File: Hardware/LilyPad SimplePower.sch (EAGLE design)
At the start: 22 parts, among them U1 MCP73831

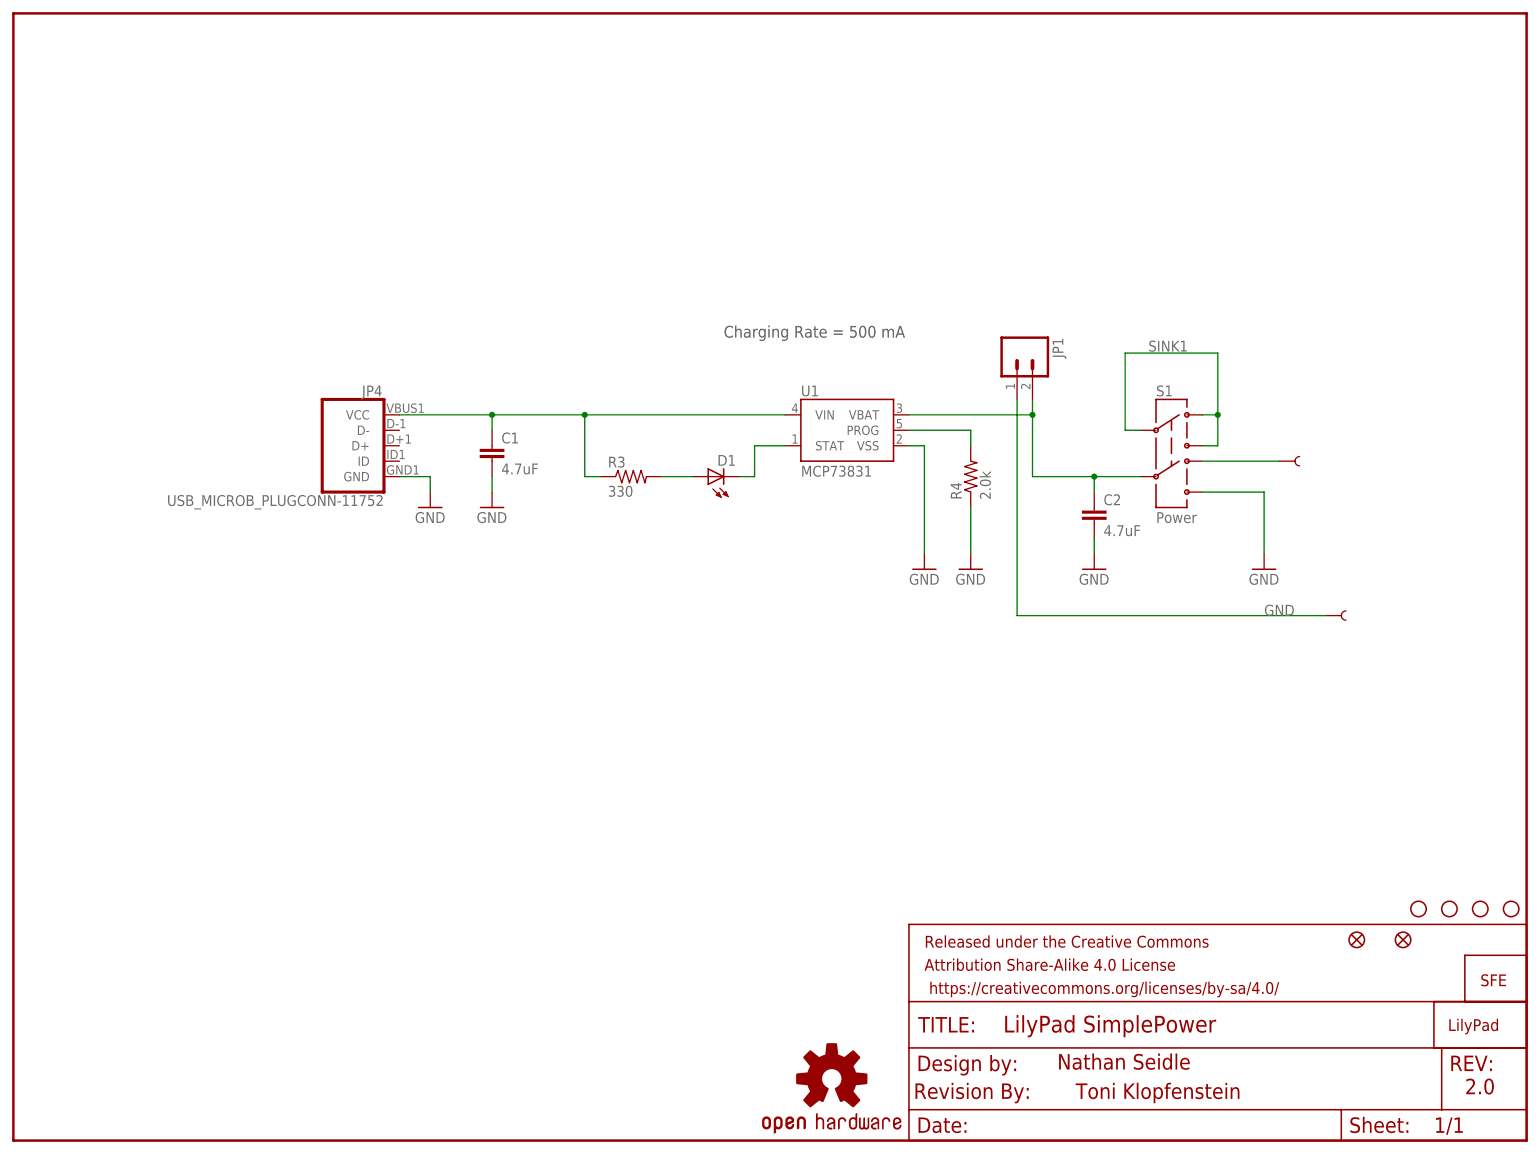
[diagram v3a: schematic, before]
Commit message: Fixing short, updating parts to match QC checklist
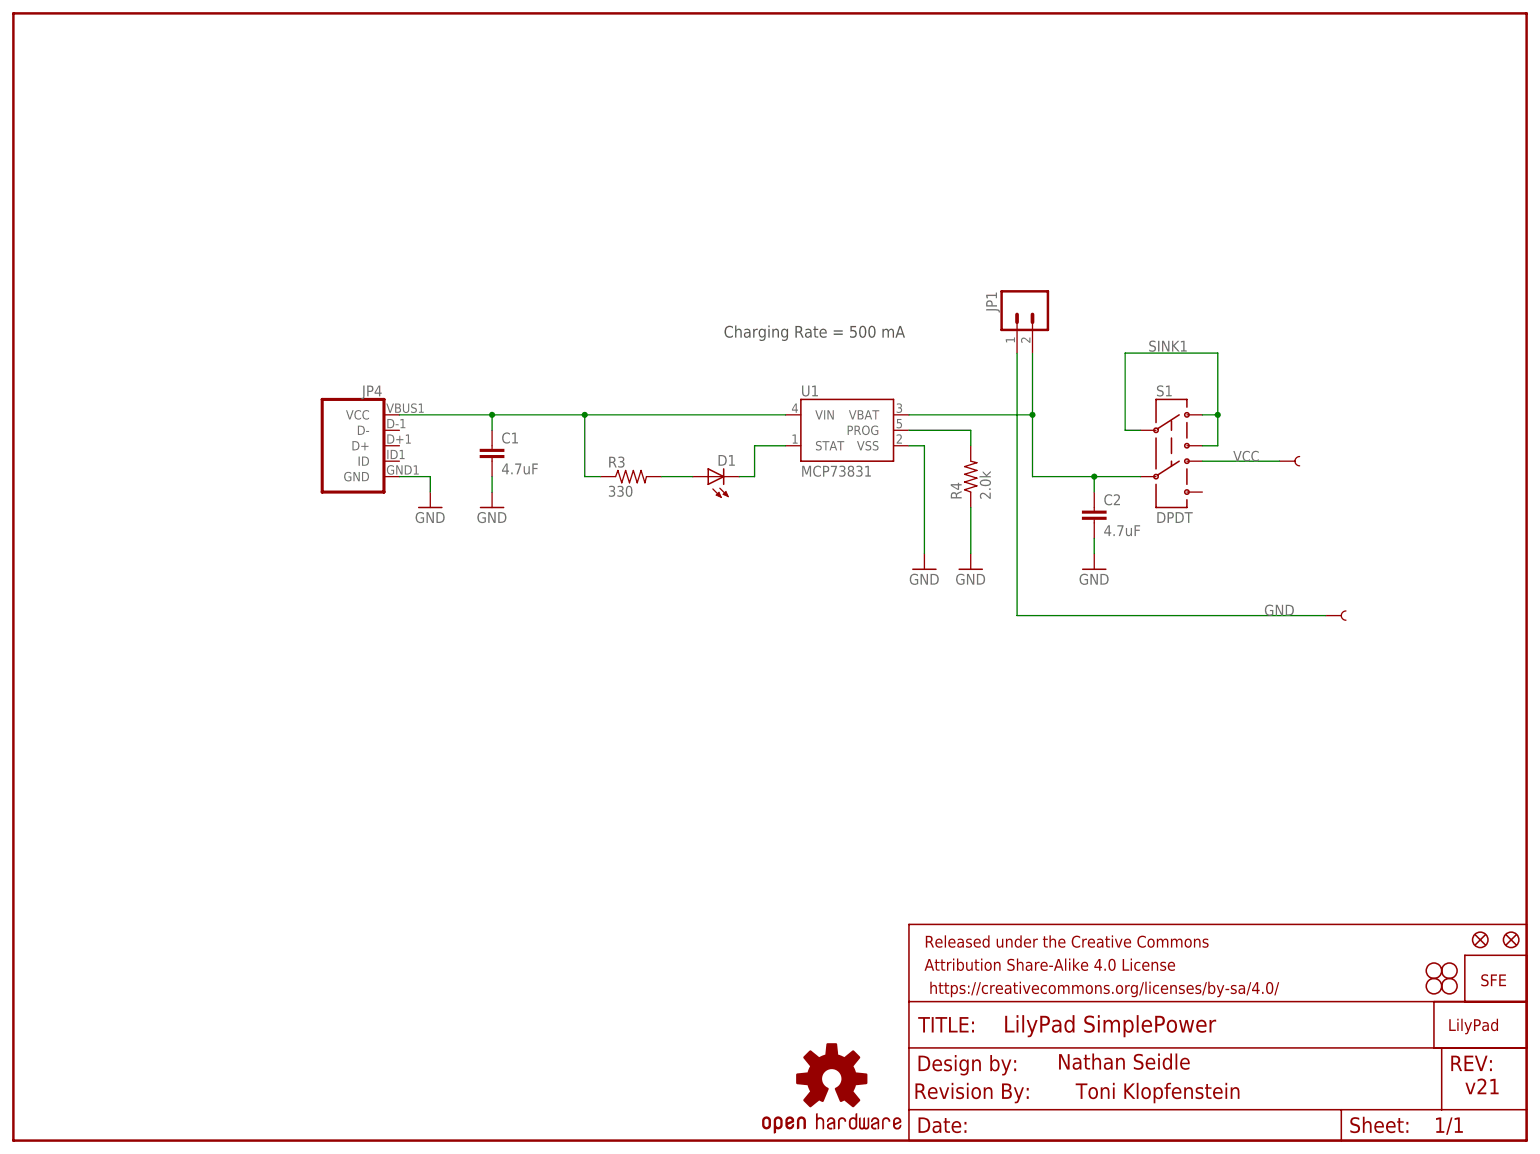
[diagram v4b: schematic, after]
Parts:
- JP1: value (none) -> M02-JST-2MM-SMT; device SparkFun:M02-JST-2MM-SMT -> SparkFun-Connectors:M02-JST-2MM-SMT
- S1: value Power -> DPDT; device SparkFun:SWITCH-DPDTSMD -> SparkFun-Electromechanical:SWITCH-DPDTAYZ0202
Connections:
- net N$6 renamed VCC
- net GND: now also JP1.2; no longer JP1.1, S1.6
- net N$1: now also JP1.1; no longer JP1.2
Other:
- note added: "v21"
- note removed: "2.0"
- moved on the sheet: JP1
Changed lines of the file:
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@@
 <?xml version="1.0" encoding="utf-8"?>
 <!DOCTYPE eagle SYSTEM "eagle.dtd">
-<eagle version="6.6.0">
+<eagle version="7.2.0">
 <drawing>
 <settings>
@@
 <layer number="56" name="wert" color="7" fill="1" visible="no" active="no"/>
 <layer number="57" name="tCAD" color="7" fill="1" visible="no" active="no"/>
+<layer number="90" name="Modules" color="5" fill="1" visible="yes" active="yes"/>
 <layer number="91" name="Nets" color="2" fill="1" visible="yes" active="yes"/>
 <layer number="92" name="Busses" color="1" fill="1" visible="yes" active="yes"/>
@@
 <layer number="254" name="cooling" color="7" fill="1" visible="yes" active="yes"/>
 </layers>
-<schematic xreflabel="%F%N/%S.%C%R" xrefpart="/%S.%C%R">
+<schematic xreflabel="%F%N/%S" xrefpart="/%S.%C%R">
 <attributes>
 </attributes>
@@
 <parts>
 <part name="FRAME1" library="SparkFun-Aesthetics" deviceset="FRAME-LETTER" device=""/>
-<part name="S1" library="SparkFun" deviceset="SWITCH-DPDT" device="SMD" value="Power"/>
-<part name="JP1" library="SparkFun" deviceset="M02" device="-JST-2MM-SMT"/>
+<part name="S1" library="SparkFun-Electromechanical" deviceset="SWITCH-DPDT" device="AYZ0202" value="DPDT"/>
+<part name="JP1" library="SparkFun-Connectors" deviceset="M02" device="-JST-2MM-SMT"/>
 <part name="U$3" library="LilyPad-Wearables" deviceset="SEWTAP" device="9" value="SEWTAP9"/>
 <part name="U$4" library="LilyPad-Wearables" deviceset="SEWTAP" device="9" value="SEWTAP9"/>
@@
 <part name="STANDOFF3" library="Local Library" deviceset="SEW-HOLE-NO-PAD" device=""/>
 <part name="STANDOFF4" library="Local Library" deviceset="SEW-HOLE-NO-PAD" device=""/>
-<part name="GND6" library="SparkFun-Aesthetics" deviceset="GND" device=""/>
 <part name="FID1" library="SparkFun-Aesthetics" deviceset="FIDUCIAL" device="1X2"/>
 <part name="FID2" library="SparkFun-Aesthetics" deviceset="FIDUCIAL" device="1X2"/>
@@
 <plain>
 <text x="171.704" y="11.684" size="2.54" layer="94">Nathan Seidle</text>
-<text x="238.76" y="7.62" size="2.54" layer="94">2.0</text>
+<text x="238.76" y="7.62" size="2.54" layer="94">v21</text>
 <text x="174.752" y="6.858" size="2.54" layer="94">Toni Klopfenstein</text>
 <text x="116.84" y="132.08" size="1.9304" layer="97">Charging Rate = 500 mA</text>
@@
 <instance part="FRAME1" gate="G$2" x="147.32" y="0"/>
 <instance part="S1" gate="G$1" x="190.5" y="114.3"/>
-<instance part="JP1" gate="G$1" x="165.1" y="129.54" rot="R270"/>
+<instance part="JP1" gate="G$1" x="167.64" y="137.16" smashed="yes" rot="MR270">
+<attribute name="NAME" x="161.798" y="139.7" size="1.778" layer="95" rot="MR270"/>
+</instance>
 <instance part="U$3" gate="G$1" x="218.44" y="86.36"/>
 <instance part="U$4" gate="G$1" x="210.82" y="111.76"/>
@@
 <instance part="JP3" gate="G$1" x="241.3" y="25.4"/>
 <instance part="U1" gate="G$1" x="137.16" y="116.84"/>
-<instance part="JP4" gate="G$1" x="55.88" y="114.3" rot="MR0"/>
+<instance part="JP4" gate="G$1" x="55.88" y="114.3" smashed="yes" rot="MR0">
+<attribute name="NAME" x="60.706" y="122.428" size="1.778" layer="95" rot="MR0"/>
+</instance>
 <instance part="GND1" gate="1" x="68.58" y="104.14"/>
 <instance part="C1" gate="G$1" x="78.74" y="111.76"/>
@@
 <instance part="U$6" gate="G$1" x="148.082" y="6.858"/>
 <instance part="U$1" gate="G$1" x="236.22" y="17.78"/>
-<instance part="STANDOFF1" gate="G$1" x="246.38" y="38.1"/>
-<instance part="STANDOFF2" gate="G$1" x="241.3" y="38.1"/>
-<instance part="STANDOFF3" gate="G$1" x="236.22" y="38.1"/>
-<instance part="STANDOFF4" gate="G$1" x="231.14" y="38.1"/>
-<instance part="GND6" gate="1" x="205.74" y="93.98"/>
-<instance part="FID1" gate="G$1" x="220.98" y="33.02"/>
-<instance part="FID2" gate="G$1" x="228.6" y="33.02"/>
+<instance part="STANDOFF1" gate="G$1" x="236.22" y="27.94"/>
+<instance part="STANDOFF2" gate="G$1" x="233.68" y="27.94"/>
+<instance part="STANDOFF3" gate="G$1" x="233.68" y="25.4"/>
+<instance part="STANDOFF4" gate="G$1" x="236.22" y="25.4"/>
+<instance part="FID1" gate="G$1" x="246.38" y="33.02"/>
+<instance part="FID2" gate="G$1" x="241.3" y="33.02"/>
 </instances>
 <busses>
@@
 <net name="GND" class="0">
 <segment>
-<wire x1="165.1" y1="121.92" x2="165.1" y2="86.36" width="0.1524" layer="91"/>
 <wire x1="165.1" y1="86.36" x2="215.9" y2="86.36" width="0.1524" layer="91"/>
 <label x="205.74" y="86.36" size="1.778" layer="95"/>
-<pinref part="JP1" gate="G$1" pin="1"/>
 <pinref part="U$3" gate="G$1" pin="1"/>
+<pinref part="JP1" gate="G$1" pin="2"/>
+<wire x1="165.1" y1="86.36" x2="165.1" y2="129.54" width="0.1524" layer="91"/>
 </segment>
 <segment>
@@
 <wire x1="157.48" y1="104.14" x2="157.48" y2="96.52" width="0.1524" layer="91"/>
 </segment>
-<segment>
-<wire x1="195.58" y1="106.68" x2="205.74" y2="106.68" width="0.1524" layer="91"/>
-<pinref part="S1" gate="G$1" pin="6"/>
-<pinref part="GND6" gate="1" pin="GND"/>
-<wire x1="205.74" y1="106.68" x2="205.74" y2="96.52" width="0.2032" layer="91"/>
-</segment>
 </net>
 <net name="N$1" class="0">
@@
 <wire x1="167.64" y1="119.38" x2="167.64" y2="109.22" width="0.1524" layer="91"/>
 <wire x1="167.64" y1="109.22" x2="177.8" y2="109.22" width="0.1524" layer="91"/>
-<pinref part="JP1" gate="G$1" pin="2"/>
 <pinref part="S1" gate="G$1" pin="5"/>
 <pinref part="C2" gate="G$1" pin="1"/>
@@
 <pinref part="U1" gate="G$1" pin="VBAT"/>
 <wire x1="147.32" y1="119.38" x2="167.64" y2="119.38" width="0.1524" layer="91"/>
-<wire x1="167.64" y1="119.38" x2="167.64" y2="121.92" width="0.1524" layer="91"/>
+<pinref part="JP1" gate="G$1" pin="1"/>
+<wire x1="167.64" y1="129.54" x2="167.64" y2="119.38" width="0.1524" layer="91"/>
 <junction x="167.64" y="119.38"/>
 </segment>
@@
 </segment>
 </net>
-<net name="N$6" class="0">
+<net name="VCC" class="0">
 <segment>
 <wire x1="195.58" y1="111.76" x2="208.28" y2="111.76" width="0.1524" layer="91"/>
 <pinref part="S1" gate="G$1" pin="4"/>
 <pinref part="U$4" gate="G$1" pin="1"/>
-</segment>
-</net>
+<label x="200.66" y="111.76" size="1.6764" layer="95"/>
+</segment>
+</net>
